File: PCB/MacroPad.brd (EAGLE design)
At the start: 76.2 x 76.2 mm, 42 parts, among them SW01 KEYSWITCH-PLAIN-MX-1U, SW02 KEYSWITCH-PLAIN-MX-1U, SW03 KEYSWITCH-PLAIN-MX-1U, SW04 KEYSWITCH-PLAIN-MX-1U, SW05 KEYSWITCH-PLAIN-MX-1U, SW06 KEYSWITCH-PLAIN-MX-1U, SW07 KEYSWITCH-PLAIN-MX-1U, SW08 KEYSWITCH-PLAIN-MX-1U, SW09 KEYSWITCH-PLAIN-MX-1U, SW10 KEYSWITCH-PLAIN-MX-1U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

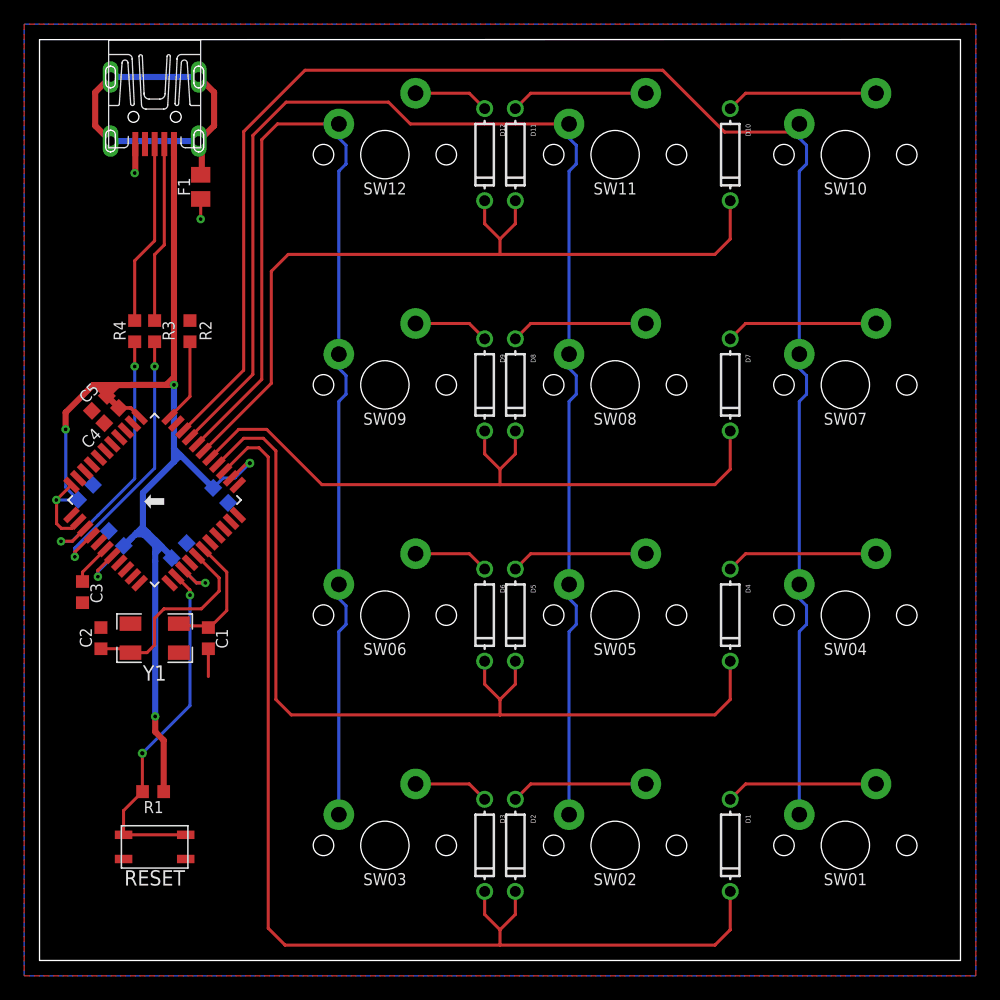
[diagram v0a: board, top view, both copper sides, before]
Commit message: Finishing Touches: Date, cam file, row 2 routing, chip orientation indicator
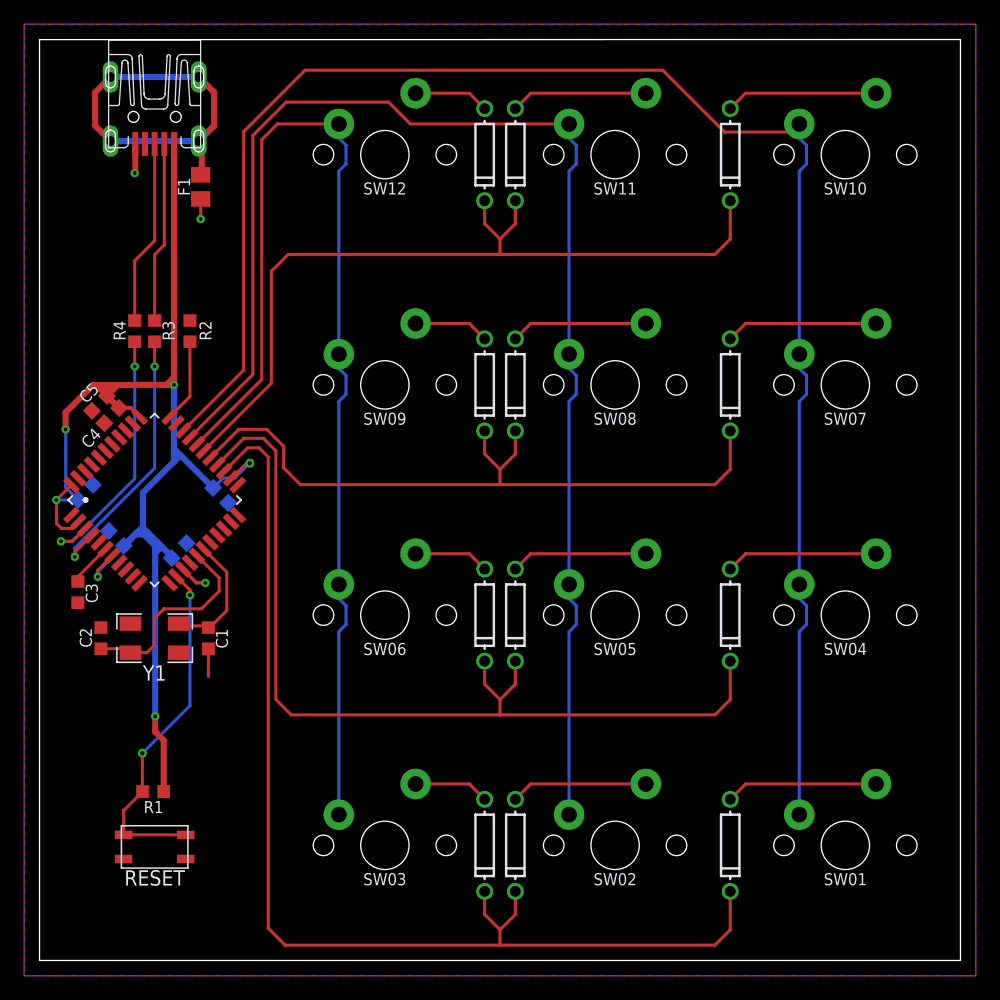
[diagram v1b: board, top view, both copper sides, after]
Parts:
- moved C3 0.38 mm to (3.17, 30.5)
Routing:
- net N$32: track 58.2 -> 59.3 mm
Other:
- board text added: "v20190608"
- board text removed: "v20190525"
- board text removed: "⬅"
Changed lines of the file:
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@@
 <wire x1="76.2" y1="76.2" x2="0" y2="76.19" width="0" layer="20"/>
 <wire x1="0" y1="76.19" x2="0" y2="0" width="0" layer="20"/>
-<text x="38.1" y="2.54" size="1.778" layer="22" rot="MR0" align="bottom-center">v20190525</text>
-<text x="9.525" y="38.1" size="1.778" layer="25" align="center">⬅</text>
+<text x="38.1" y="2.54" size="1.778" layer="22" rot="MR0" align="bottom-center">v20190608</text>
+<circle x="3.81" y="38.1" radius="0.127" width="0.254" layer="21"/>
 </plain>
 <attributes>
@@
 <attribute name="OC_NEWARK" value="unknown" x="14.986" y="38.481" size="1.778" layer="28" rot="MR225" display="off"/>
 </element>
-<element name="C3" library="Components" package="C0603" value="1u" x="3.556" y="30.48" smashed="yes" rot="R270">
-<attribute name="MF" value="" x="3.556" y="30.48" size="1.778" layer="27" rot="R270" display="off"/>
-<attribute name="MPN" value="" x="3.556" y="30.48" size="1.778" layer="27" rot="R270" display="off"/>
-<attribute name="NAME" x="4.206" y="30.391" size="1" layer="25" ratio="13" rot="R270" align="bottom-center"/>
-<attribute name="OC_NEWARK" value="unknown" x="3.556" y="30.48" size="1.778" layer="27" rot="R270" display="off"/>
+<element name="C3" library="Components" package="C0603" value="1u" x="3.175" y="30.48" smashed="yes" rot="R270">
+<attribute name="MF" value="" x="3.175" y="30.48" size="1.778" layer="27" rot="R270" display="off"/>
+<attribute name="MPN" value="" x="3.175" y="30.48" size="1.778" layer="27" rot="R270" display="off"/>
+<attribute name="NAME" x="3.825" y="30.391" size="1" layer="25" ratio="13" rot="R270" align="bottom-center"/>
+<attribute name="OC_NEWARK" value="unknown" x="3.175" y="30.48" size="1.778" layer="27" rot="R270" display="off"/>
 </element>
 <element name="F1" library="USB" package="F0805" value="" x="13.335" y="64.008" smashed="yes" rot="R90">
@@
 </element>
 <element name="D12" library="adafruit" library_urn="urn:adsk.eagle:library:420" package="DO-1N4148" package3d_urn="urn:adsk.eagle:package:6240748/1" value="" x="36.83" y="66.675" smashed="yes" rot="R270">
-<attribute name="NAME" x="38.1" y="69.215" size="0.4064" layer="25" rot="R270"/>
 <attribute name="VALUE" x="36.576" y="68.707" size="0.6096" layer="21" rot="R270"/>
 </element>
 <element name="D1" library="adafruit" library_urn="urn:adsk.eagle:library:420" package="DO-1N4148" package3d_urn="urn:adsk.eagle:package:6240748/1" value="" x="57.15" y="9.525" smashed="yes" rot="R270">
-<attribute name="NAME" x="58.42" y="12.065" size="0.4064" layer="25" rot="R270"/>
 <attribute name="VALUE" x="56.896" y="11.557" size="0.6096" layer="21" rot="R270"/>
 </element>
 <element name="D2" library="adafruit" library_urn="urn:adsk.eagle:library:420" package="DO-1N4148" package3d_urn="urn:adsk.eagle:package:6240748/1" value="" x="39.37" y="9.525" smashed="yes" rot="R270">
-<attribute name="NAME" x="40.64" y="12.065" size="0.4064" layer="25" rot="R270"/>
 <attribute name="VALUE" x="39.116" y="11.557" size="0.6096" layer="21" rot="R270"/>
 </element>
 <element name="D3" library="adafruit" library_urn="urn:adsk.eagle:library:420" package="DO-1N4148" package3d_urn="urn:adsk.eagle:package:6240748/1" value="" x="36.83" y="9.525" smashed="yes" rot="R270">
-<attribute name="NAME" x="38.1" y="12.065" size="0.4064" layer="25" rot="R270"/>
 <attribute name="VALUE" x="36.576" y="11.557" size="0.6096" layer="21" rot="R270"/>
 </element>
 <element name="D4" library="adafruit" library_urn="urn:adsk.eagle:library:420" package="DO-1N4148" package3d_urn="urn:adsk.eagle:package:6240748/1" value="" x="57.15" y="28.575" smashed="yes" rot="R270">
-<attribute name="NAME" x="58.42" y="31.115" size="0.4064" layer="25" rot="R270"/>
 <attribute name="VALUE" x="56.896" y="30.607" size="0.6096" layer="21" rot="R270"/>
 </element>
 <element name="D5" library="adafruit" library_urn="urn:adsk.eagle:library:420" package="DO-1N4148" package3d_urn="urn:adsk.eagle:package:6240748/1" value="" x="39.37" y="28.575" smashed="yes" rot="R270">
-<attribute name="NAME" x="40.64" y="31.115" size="0.4064" layer="25" rot="R270"/>
 <attribute name="VALUE" x="39.116" y="30.607" size="0.6096" layer="21" rot="R270"/>
 </element>
 <element name="D6" library="adafruit" library_urn="urn:adsk.eagle:library:420" package="DO-1N4148" package3d_urn="urn:adsk.eagle:package:6240748/1" value="" x="36.83" y="28.575" smashed="yes" rot="R270">
-<attribute name="NAME" x="38.1" y="31.115" size="0.4064" layer="25" rot="R270"/>
 <attribute name="VALUE" x="36.576" y="30.607" size="0.6096" layer="21" rot="R270"/>
 </element>
 <element name="D7" library="adafruit" library_urn="urn:adsk.eagle:library:420" package="DO-1N4148" package3d_urn="urn:adsk.eagle:package:6240748/1" value="" x="57.15" y="47.625" smashed="yes" rot="R270">
-<attribute name="NAME" x="58.42" y="50.165" size="0.4064" layer="25" rot="R270"/>
 <attribute name="VALUE" x="56.896" y="49.657" size="0.6096" layer="21" rot="R270"/>
 </element>
 <element name="D8" library="adafruit" library_urn="urn:adsk.eagle:library:420" package="DO-1N4148" package3d_urn="urn:adsk.eagle:package:6240748/1" value="" x="39.37" y="47.625" smashed="yes" rot="R270">
-<attribute name="NAME" x="40.64" y="50.165" size="0.4064" layer="25" rot="R270"/>
 <attribute name="VALUE" x="39.116" y="49.657" size="0.6096" layer="21" rot="R270"/>
 </element>
 <element name="D9" library="adafruit" library_urn="urn:adsk.eagle:library:420" package="DO-1N4148" package3d_urn="urn:adsk.eagle:package:6240748/1" value="" x="36.83" y="47.625" smashed="yes" rot="R270">
-<attribute name="NAME" x="38.1" y="50.165" size="0.4064" layer="25" rot="R270"/>
 <attribute name="VALUE" x="36.576" y="49.657" size="0.6096" layer="21" rot="R270"/>
 </element>
 <element name="D10" library="adafruit" library_urn="urn:adsk.eagle:library:420" package="DO-1N4148" package3d_urn="urn:adsk.eagle:package:6240748/1" value="" x="57.15" y="66.675" smashed="yes" rot="R270">
-<attribute name="NAME" x="58.42" y="69.215" size="0.4064" layer="25" rot="R270"/>
 <attribute name="VALUE" x="56.896" y="68.707" size="0.6096" layer="21" rot="R270"/>
 </element>
 <element name="D11" library="adafruit" library_urn="urn:adsk.eagle:library:420" package="DO-1N4148" package3d_urn="urn:adsk.eagle:package:6240748/1" value="" x="39.37" y="66.675" smashed="yes" rot="R270">
-<attribute name="NAME" x="40.64" y="69.215" size="0.4064" layer="25" rot="R270"/>
 <attribute name="VALUE" x="39.116" y="68.707" size="0.6096" layer="21" rot="R270"/>
 </element>
@@
 <signal name="UCAP">
 <contactref element="C3" pad="1"/>
-<wire x1="3.556" y1="32.131" x2="3.556" y2="31.355" width="0.254" layer="1"/>
+<wire x1="3.175" y1="31.75" x2="3.175" y2="31.355" width="0.254" layer="1"/>
 <contactref element="U1" pad="6"/>
-<wire x1="5.465921875" y1="34.040921875" x2="3.556" y2="32.131" width="0.254" layer="1"/>
+<wire x1="5.465921875" y1="34.040921875" x2="3.175" y2="31.75" width="0.254" layer="1"/>
 </signal>
 <signal name="N$5">
@@
 <contactref element="D8" pad="C"/>
 <contactref element="D7" pad="C"/>
-<wire x1="23.368" y1="39.37" x2="38.1" y2="39.37" width="0.254" layer="1"/>
 <wire x1="38.1" y1="39.37" x2="55.88" y2="39.37" width="0.254" layer="1"/>
 <wire x1="55.88" y1="39.37" x2="57.15" y2="40.64" width="0.254" layer="1"/>
@@
 <contactref element="U1" pad="27"/>
 <wire x1="14.14085" y1="41.602296875" x2="16.480553125" y2="43.942" width="0.254" layer="1"/>
-<wire x1="16.480553125" y1="43.942" x2="18.796" y2="43.942" width="0.254" layer="1"/>
-<wire x1="18.796" y1="43.942" x2="23.368" y2="39.37" width="0.254" layer="1"/>
+<wire x1="18.796" y1="43.942" x2="16.480553125" y2="43.942" width="0.254" layer="1"/>
+<wire x1="18.796" y1="43.942" x2="20.193" y2="42.545" width="0.254" layer="1"/>
+<wire x1="21.59" y1="39.37" x2="20.193" y2="40.767" width="0.254" layer="1"/>
+<wire x1="20.193" y1="40.767" x2="20.193" y2="42.545" width="0.254" layer="1"/>
+<wire x1="38.1" y1="39.37" x2="21.59" y2="39.37" width="0.254" layer="1"/>
 </signal>
 <signal name="N$33">

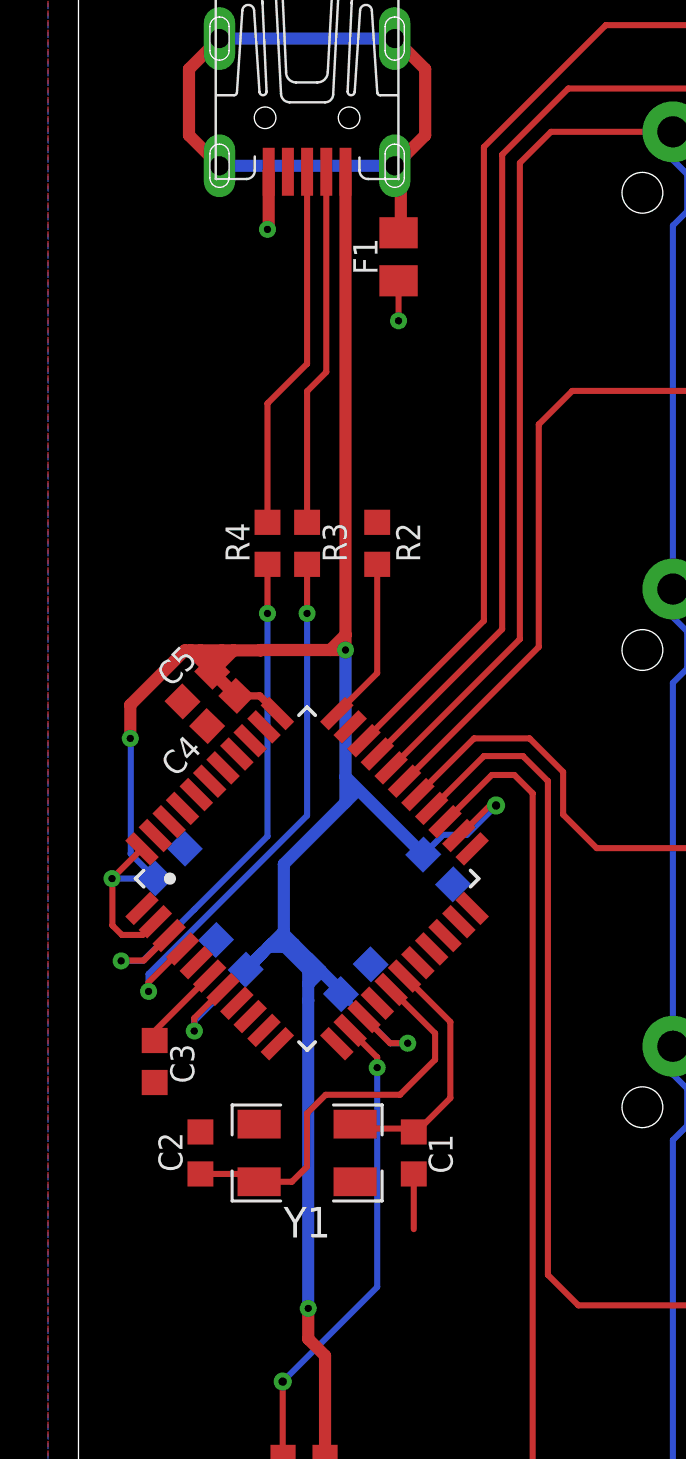
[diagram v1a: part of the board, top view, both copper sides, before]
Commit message: Use ATMEGA32U4-AU
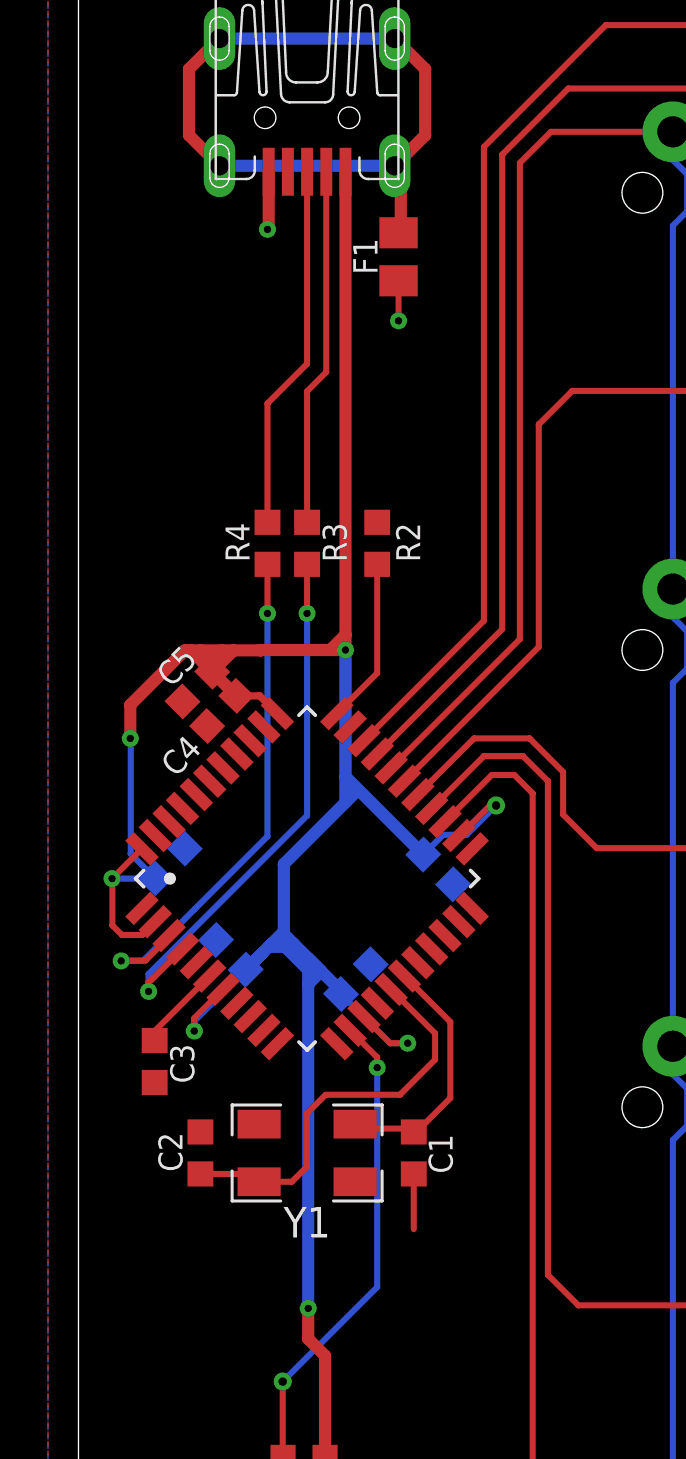
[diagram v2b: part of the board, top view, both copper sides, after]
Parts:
- U1: value ATMEGA32U4-AUR -> ATMEGA32U4-AU; device ATMEGA32U4-AUR:QFP80P1200X1200X120-44N -> ATMEGA32U4-AU:QFP80P1200X1200X120-44N

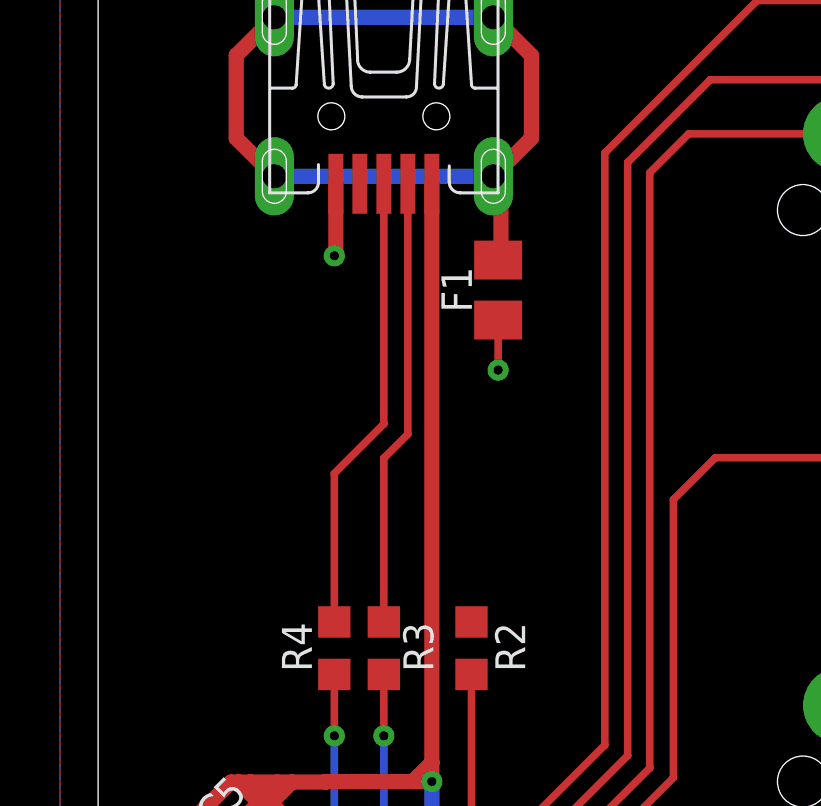
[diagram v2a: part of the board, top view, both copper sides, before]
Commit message: Update PCB to correct D- and D+ mapping. Increment Date
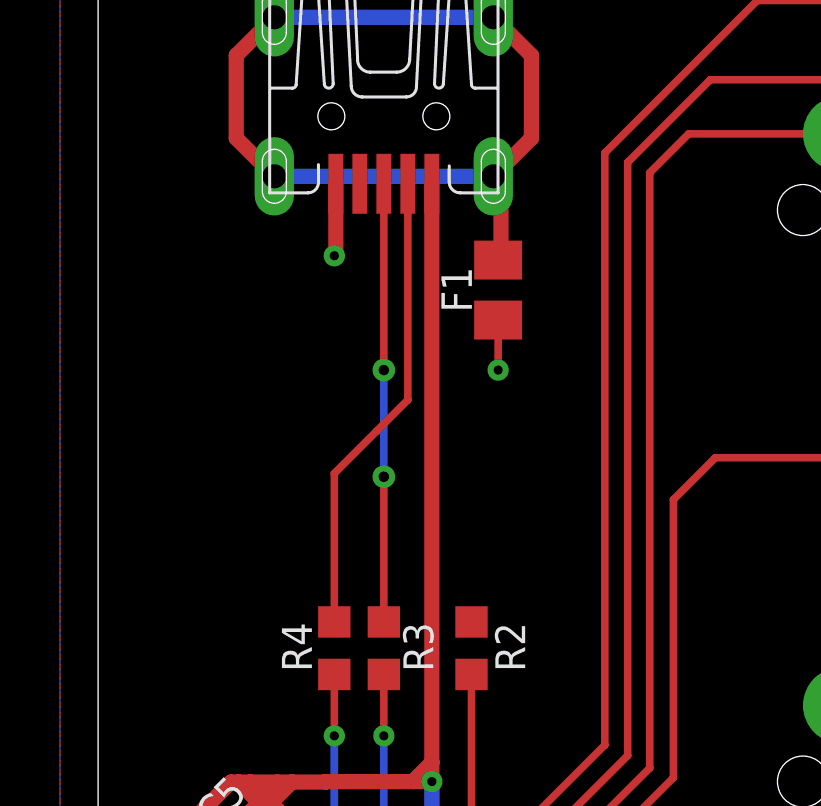
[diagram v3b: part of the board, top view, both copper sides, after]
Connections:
- net N$5: now also USB1.D-; no longer USB1.D+
- net N$7: now also USB1.D+; no longer USB1.D-
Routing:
- net N$7: track 14.9 -> 14.6 mm, vias 0 -> 2
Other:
- board text added: "v20190619"
- board text removed: "v20190608"
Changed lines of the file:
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@@
 <wire x1="76.2" y1="76.2" x2="0" y2="76.19" width="0" layer="20"/>
 <wire x1="0" y1="76.19" x2="0" y2="0" width="0" layer="20"/>
-<text x="38.1" y="2.54" size="1.778" layer="22" rot="MR0" align="bottom-center">v20190608</text>
+<text x="38.1" y="2.54" size="1.778" layer="22" rot="MR0" align="bottom-center">v20190619</text>
 <circle x="3.81" y="38.1" radius="0.127" width="0.254" layer="21"/>
 </plain>
@@
 </signal>
 <signal name="N$5">
-<contactref element="USB1" pad="D+"/>
 <contactref element="R4" pad="1"/>
-<wire x1="9.525" y1="67.55" x2="9.525" y2="59.549" width="0.254" layer="1"/>
-<wire x1="9.525" y1="59.549" x2="7.874" y2="57.898" width="0.254" layer="1"/>
+<wire x1="9.525" y1="59.549" x2="9.278" y2="59.302" width="0.254" layer="1"/>
+<wire x1="9.278" y1="59.302" x2="7.874" y2="57.898" width="0.254" layer="1"/>
 <wire x1="7.874" y1="57.898" x2="7.874" y2="52.945" width="0.254" layer="1"/>
+<contactref element="USB1" pad="D-"/>
+<wire x1="9.525" y1="59.549" x2="10.325" y2="60.349" width="0.254" layer="1"/>
+<wire x1="10.325" y1="60.349" x2="10.325" y2="67.55" width="0.254" layer="1"/>
 </signal>
 <signal name="N$6">
@@
 </signal>
 <signal name="N$7">
-<contactref element="USB1" pad="D-"/>
 <contactref element="R3" pad="1"/>
-<wire x1="10.325" y1="67.55" x2="10.325" y2="59.206" width="0.254" layer="1"/>
-<wire x1="9.525" y1="52.945" x2="9.525" y2="58.406" width="0.254" layer="1"/>
-<wire x1="10.325" y1="59.206" x2="9.525" y2="58.406" width="0.254" layer="1"/>
+<contactref element="USB1" pad="D+"/>
+<wire x1="9.525" y1="52.945" x2="9.525" y2="57.785" width="0.254" layer="1"/>
+<via x="9.525" y="57.785" extent="1-16" drill="0.35"/>
+<wire x1="9.525" y1="57.785" x2="9.525" y2="61.341" width="0.254" layer="16"/>
+<via x="9.525" y="61.341" extent="1-16" drill="0.35"/>
+<wire x1="9.525" y1="61.341" x2="9.525" y2="67.55" width="0.254" layer="1"/>
 </signal>
 <signal name="N$8">
